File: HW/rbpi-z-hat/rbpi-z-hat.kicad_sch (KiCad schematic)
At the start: 0 parts

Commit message: Some new things...
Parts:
- added U7: STM32F031G6Ux, Package_DFN_QFN:QFN-28-1EP_4x4mm_P0.4mm_EP2.6x2.6mm_ThermalVias, symbol MCU_ST_STM32F0:STM32F031G6Ux
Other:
- note added: "CH32V203G6U6"

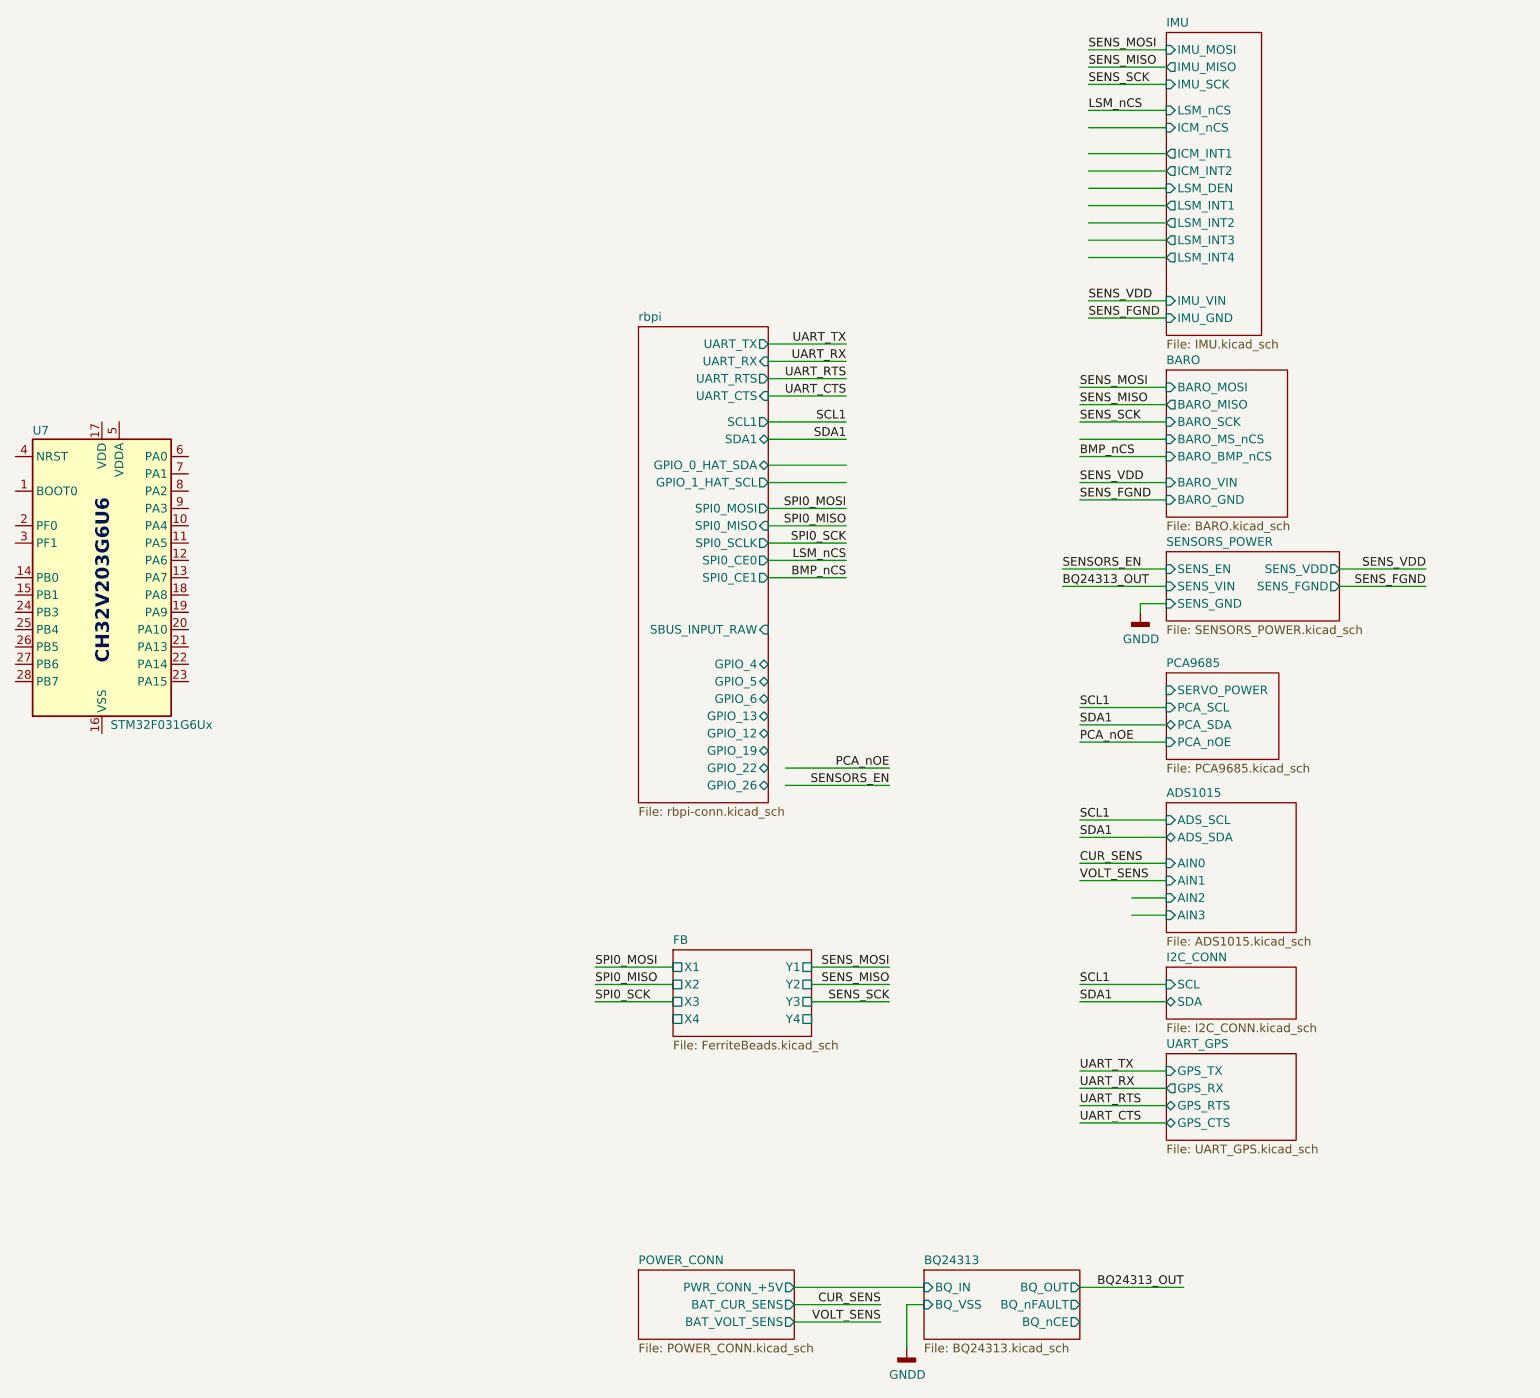
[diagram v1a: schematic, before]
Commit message: PCA and ADC replaced by CH32V203G6U6
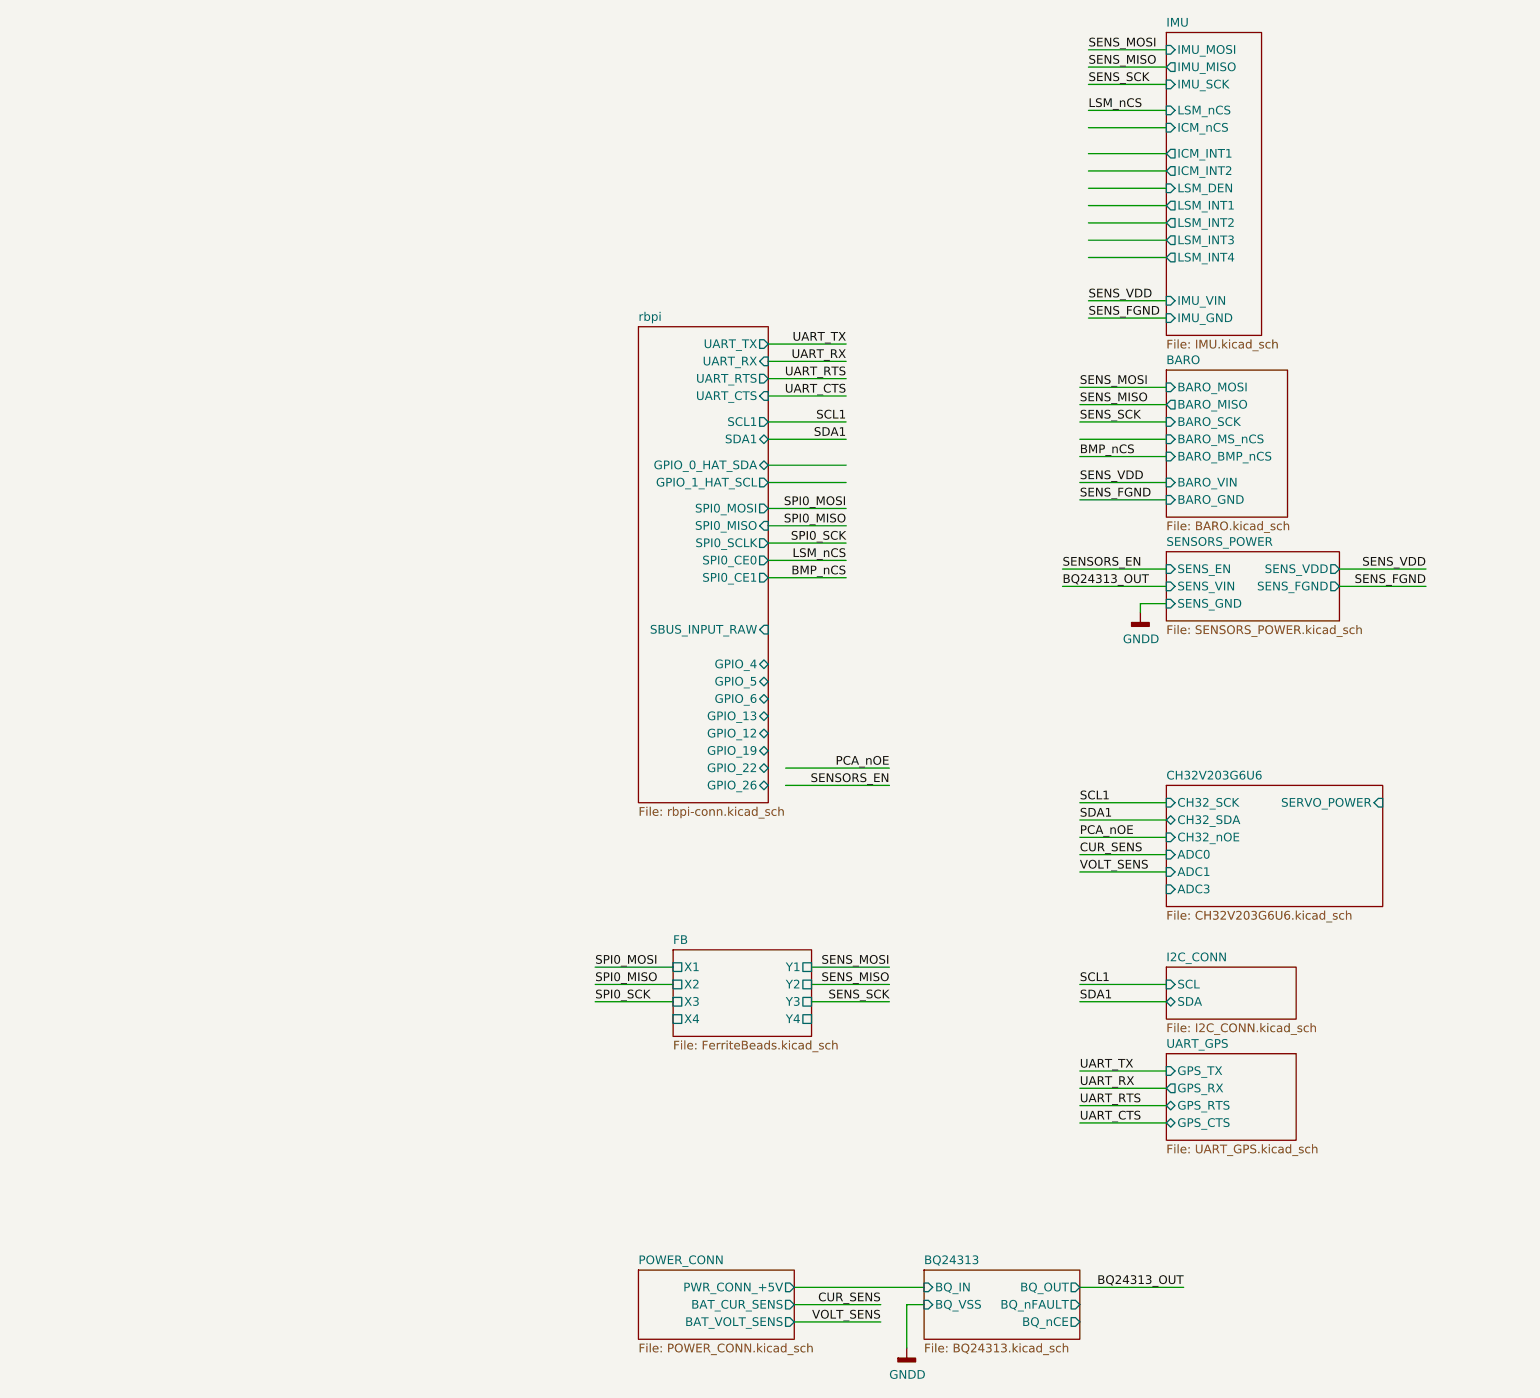
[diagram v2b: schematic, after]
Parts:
- removed U7: STM32F031G6Ux, Package_DFN_QFN:QFN-28-1EP_4x4mm_P0.4mm_EP2.6x2.6mm_ThermalVias, symbol MCU_ST_STM32F0:STM32F031G6Ux
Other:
- removed sheet ADS1015
- removed sheet PCA9685
- added sheet CH32V203G6U6 (CH32V203G6U6.kicad_sch)
- note removed: "CH32V203G6U6"

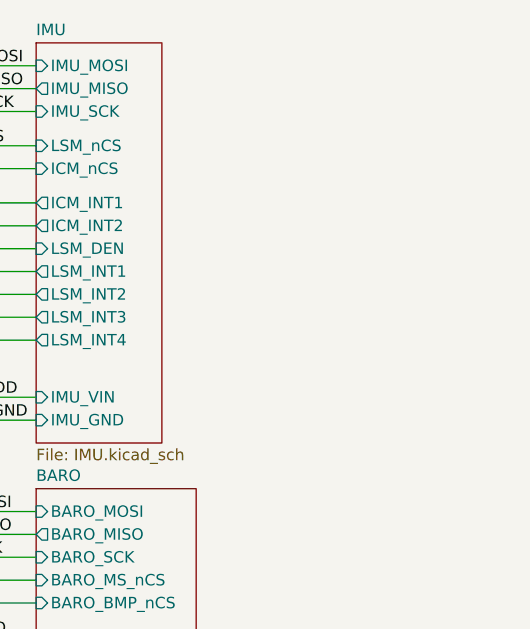
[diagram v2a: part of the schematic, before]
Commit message: Added schematics for IST8310
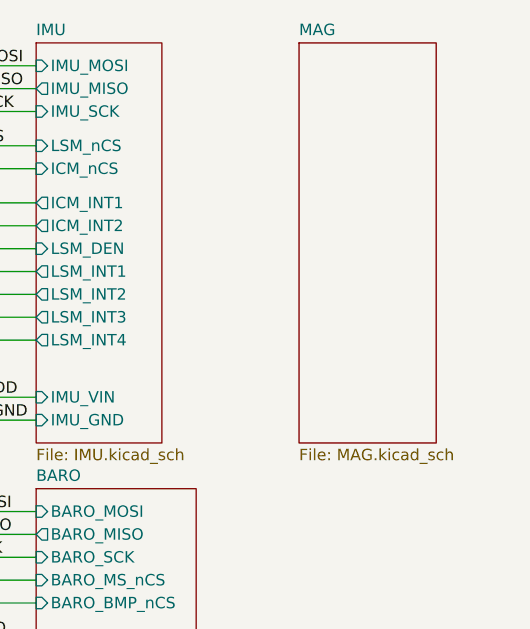
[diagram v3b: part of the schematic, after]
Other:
- added sheet MAG (MAG.kicad_sch)
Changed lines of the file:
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@@
+    )
+  )
+  (sheet (at 161.29 19.05) (size 15.24 44.45) (fields_autoplaced)
+    (stroke (width 0.1524) (type solid))
+    (fill (color 0 0 0 0.0000))
+    (property "Sheetname" "MAG" (at 161.29 18.3384 0)
+      (effects (font (size 1.27 1.27)) (justify left bottom))
+    )
+    (property "Sheetfile" "MAG.kicad_sch" (at 161.29 64.0846 0)
+      (effects (font (size 1.27 1.27)) (justify left top))
+    )
+    (instances
+      (project "rbpi-z-hat"
+        (path "/d99b0340-d795-4b40-9cde-9851c6cee99d" (page "17"))
+      )
     )
   )

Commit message: Apdated Sch and PCB
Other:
- sheet MAG ports: added MAG_GND, MAG_IST_DRDY, MAG_IST_nRST, MAG_QMC_INT, MAG_SCL, MAG_SDA, MAG_VDD; removed none
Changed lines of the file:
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@@
+    (stroke (width 0) (type default))
+  )
+  (wire (pts (xy 161.29 40.64) (xy 149.86 40.64))
     (stroke (width 0) (type default))
   )
@@
     (stroke (width 0) (type default))
   )
+  (wire (pts (xy 161.29 38.1) (xy 149.86 38.1))
+    (stroke (width 0) (type default))
+  )
   (wire (pts (xy 73.66 76.2) (xy 85.09 76.2))
     (stroke (width 0) (type default))
@@
     (stroke (width 0) (type default))
   )
+  (wire (pts (xy 149.86 21.59) (xy 161.29 21.59))
+    (stroke (width 0) (type default))
+  )
   (wire (pts (xy 76.2 129.54) (xy 91.44 129.54))
     (stroke (width 0) (type default))
@@
     (stroke (width 0) (type default))
   )
+  (wire (pts (xy 149.86 24.13) (xy 161.29 24.13))
+    (stroke (width 0) (type default))
+  )
   (wire (pts (xy 73.66 82.55) (xy 85.09 82.55))
     (stroke (width 0) (type default))
@@
     (effects (font (size 1.27 1.27)) (justify left bottom))
   )
+  (label "SENS_FGND" (at 149.86 40.64 0) (fields_autoplaced)
+    (effects (font (size 1.27 1.27)) (justify left bottom))
+  )
   (label "UART_RTS" (at 85.09 69.85 180) (fields_autoplaced)
     (effects (font (size 1.27 1.27)) (justify right bottom))
@@
     (effects (font (size 1.27 1.27)) (justify left bottom))
   )
+  (label "SCL1" (at 149.86 24.13 0) (fields_autoplaced)
+    (effects (font (size 1.27 1.27)) (justify left bottom))
+  )
   (label "SDA1" (at 119.38 134.62 0) (fields_autoplaced)
     (effects (font (size 1.27 1.27)) (justify left bottom))
@@
     (effects (font (size 1.27 1.27)) (justify right bottom))
   )
+  (label "SENS_VDD" (at 149.86 38.1 0) (fields_autoplaced)
+    (effects (font (size 1.27 1.27)) (justify left bottom))
+  )
   (label "BMP_nCS" (at 119.38 81.28 0) (fields_autoplaced)
     (effects (font (size 1.27 1.27)) (justify left bottom))
@@
   )
   (label "SENS_FGND" (at 120.65 60.96 0) (fields_autoplaced)
+    (effects (font (size 1.27 1.27)) (justify left bottom))
+  )
+  (label "SDA1" (at 149.86 21.59 0) (fields_autoplaced)
     (effects (font (size 1.27 1.27)) (justify left bottom))
   )
@@
     )
   )
-  (sheet (at 161.29 19.05) (size 15.24 44.45) (fields_autoplaced)
+  (sheet (at 161.29 19.05) (size 20.32 24.13) (fields_autoplaced)
     (stroke (width 0.1524) (type solid))
     (fill (color 0 0 0 0.0000))
@@
       (effects (font (size 1.27 1.27)) (justify left bottom))
     )
-    (property "Sheetfile" "MAG.kicad_sch" (at 161.29 64.0846 0)
-      (effects (font (size 1.27 1.27)) (justify left top))
-    )
-    (instances
+    (property "Sheetfile" "MAG.kicad_sch" (at 161.29 43.7646 0)
+      (effects (font (size 1.27 1.27)) (justify left top))
+    )
+    (pin "MAG_SDA" bidirectional (at 161.29 21.59 180)
+      (effects (font (size 1.27 1.27)) (justify left))
+    )
+    (pin "MAG_SCL" input (at 161.29 24.13 180)
+      (effects (font (size 1.27 1.27)) (justify left))
+    )
+    (pin "MAG_IST_DRDY" output (at 161.29 27.94 180)
+      (effects (font (size 1.27 1.27)) (justify left))
+    )
+    (pin "MAG_IST_nRST" input (at 161.29 30.48 180)
+      (effects (font (size 1.27 1.27)) (justify left))
+    )
+    (pin "MAG_VDD" input (at 161.29 38.1 180)
+      (effects (font (size 1.27 1.27)) (justify left))
+    )
+    (pin "MAG_GND" input (at 161.29 40.64 180)
+      (effects (font (size 1.27 1.27)) (justify left))
+    )
+    (pin "MAG_QMC_INT" output (at 161.29 33.02 180)
+      (effects (font (size 1.27 1.27)) (justify left))
+    )
+    (instances

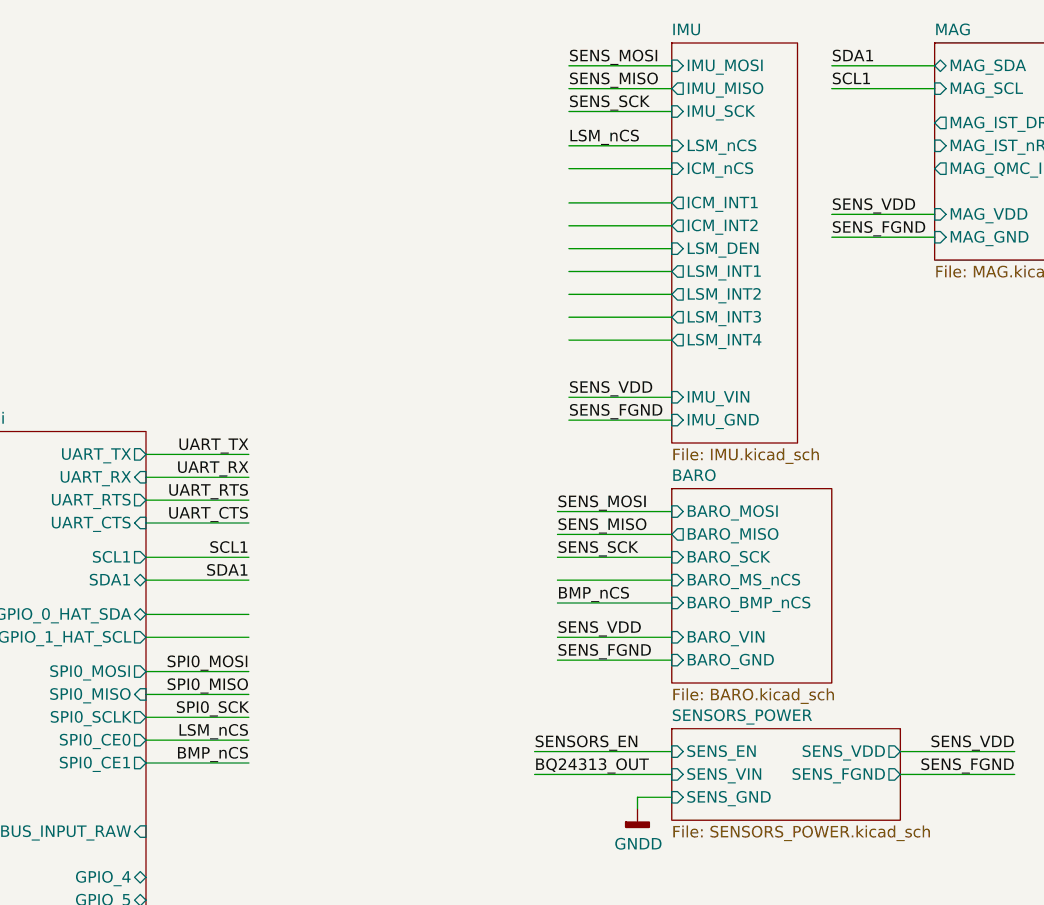
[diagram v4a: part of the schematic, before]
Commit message: Replaced LSM9DS1 with BMI160/QMI8658C
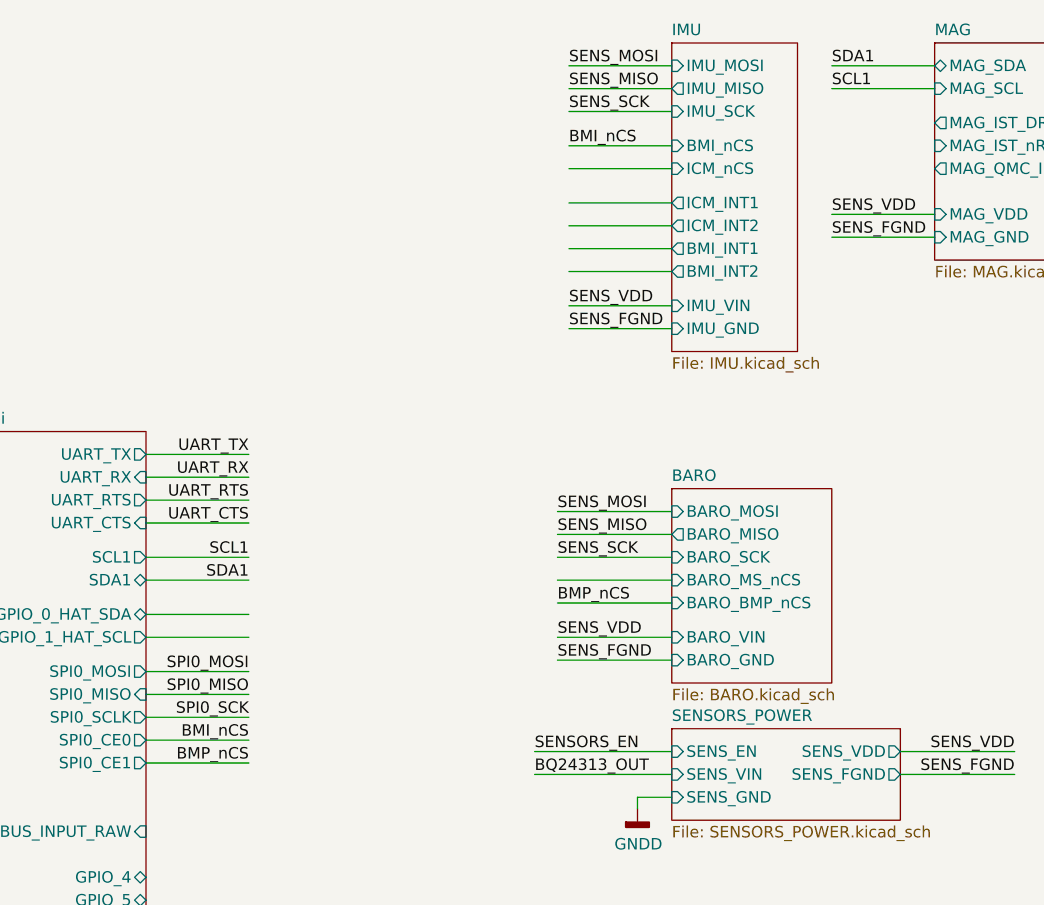
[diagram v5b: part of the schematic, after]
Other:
- sheet IMU ports: added BMI_INT1, BMI_INT2, BMI_nCS; removed LSM_DEN, LSM_INT1, LSM_INT2, LSM_INT3, LSM_INT4, LSM_nCS
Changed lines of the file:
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@@
-    (stroke (width 0) (type default))
-  )
-  (wire (pts (xy 132.08 49.53) (xy 120.65 49.53))
     (stroke (width 0) (type default))
   )
@@
     (stroke (width 0) (type default))
   )
-  (wire (pts (xy 132.08 58.42) (xy 120.65 58.42))
-    (stroke (width 0) (type default))
-  )
-  (wire (pts (xy 132.08 46.99) (xy 120.65 46.99))
+  (wire (pts (xy 132.08 48.26) (xy 120.65 48.26))
     (stroke (width 0) (type default))
   )
@@
     (stroke (width 0) (type default))
   )
-  (wire (pts (xy 132.08 52.07) (xy 120.65 52.07))
-    (stroke (width 0) (type default))
-  )
   (wire (pts (xy 132.08 30.48) (xy 120.65 30.48))
     (stroke (width 0) (type default))
@@
     (stroke (width 0) (type default))
   )
-  (wire (pts (xy 132.08 60.96) (xy 120.65 60.96))
+  (wire (pts (xy 132.08 50.8) (xy 120.65 50.8))
     (stroke (width 0) (type default))
   )
@@
     (effects (font (size 1.27 1.27)) (justify left bottom))
   )
-  (label "LSM_nCS" (at 85.09 96.52 180) (fields_autoplaced)
+  (label "BMI_nCS" (at 85.09 96.52 180) (fields_autoplaced)
     (effects (font (size 1.27 1.27)) (justify right bottom))
   )
@@
     (effects (font (size 1.27 1.27)) (justify right bottom))
   )
-  (label "SENS_VDD" (at 120.65 58.42 0) (fields_autoplaced)
+  (label "SENS_VDD" (at 120.65 48.26 0) (fields_autoplaced)
     (effects (font (size 1.27 1.27)) (justify left bottom))
   )
@@
     (effects (font (size 1.27 1.27)) (justify left bottom))
   )
-  (label "SENS_FGND" (at 120.65 60.96 0) (fields_autoplaced)
+  (label "SENS_FGND" (at 120.65 50.8 0) (fields_autoplaced)
     (effects (font (size 1.27 1.27)) (justify left bottom))
   )
@@
     (effects (font (size 1.27 1.27)) (justify left bottom))
   )
-  (label "LSM_nCS" (at 120.65 30.48 0) (fields_autoplaced)
+  (label "BMI_nCS" (at 120.65 30.48 0) (fields_autoplaced)
     (effects (font (size 1.27 1.27)) (justify left bottom))
   )
@@
     )
   )
-  (sheet (at 132.08 19.05) (size 13.97 44.45) (fields_autoplaced)
+  (sheet (at 132.08 19.05) (size 13.97 34.29) (fields_autoplaced)
     (stroke (width 0) (type solid))
     (fill (color 0 0 0 0.0000))
@@
       (effects (font (size 1.27 1.27)) (justify left bottom))
     )
-    (property "Sheetfile" "IMU.kicad_sch" (at 132.08 64.0846 0)
+    (property "Sheetfile" "IMU.kicad_sch" (at 132.08 53.9246 0)
       (effects (font (size 1.27 1.27)) (justify left top))
     )
-    (pin "IMU_VIN" input (at 132.08 58.42 180)
-      (effects (font (size 1.27 1.27)) (justify left))
-    )
-    (pin "IMU_GND" input (at 132.08 60.96 180)
-      (effects (font (size 1.27 1.27)) (justify left))
-    )
-    (pin "LSM_nCS" input (at 132.08 30.48 180)
+    (pin "IMU_VIN" input (at 132.08 48.26 180)
+      (effects (font (size 1.27 1.27)) (justify left))
+    )
+    (pin "IMU_GND" input (at 132.08 50.8 180)
       (effects (font (size 1.27 1.27)) (justify left))
     )
@@
       (effects (font (size 1.27 1.27)) (justify left))
     )
-    (pin "LSM_INT1" output (at 132.08 44.45 180)
-      (effects (font (size 1.27 1.27)) (justify left))
-    )
-    (pin "LSM_INT2" output (at 132.08 46.99 180)
-      (effects (font (size 1.27 1.27)) (justify left))
-    )
-    (pin "LSM_INT3" output (at 132.08 49.53 180)
-      (effects (font (size 1.27 1.27)) (justify left))
-    )
-    (pin "LSM_INT4" output (at 132.08 52.07 180)
-      (effects (font (size 1.27 1.27)) (justify left))
-    )
     (pin "IMU_MOSI" input (at 132.08 21.59 180)
       (effects (font (size 1.27 1.27)) (justify left))
@@
       (effects (font (size 1.27 1.27)) (justify left))
     )
-    (pin "LSM_DEN" input (at 132.08 41.91 180)
-      (effects (font (size 1.27 1.27)) (justify left))
-    )
+    (pin "BMI_nCS" input (at 132.08 30.48 180)
+      (effects (font (size 1.27 1.27)) (justify left))
+    )
+    (pin "BMI_INT1" output (at 132.08 41.91 180)
+      (effects (font (size 1.27 1.27)) (justify left))
+    )
+    (pin "BMI_INT2" output (at 132.08 44.45 180)
+      (effects (font (size 1.27 1.27)) (justify left))
+    )
